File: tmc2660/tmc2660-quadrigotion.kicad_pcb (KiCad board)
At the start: 2 copper layers, 28.4 x 34.7 mm, 16 parts, among them P3 Motor, U1 TMC2660

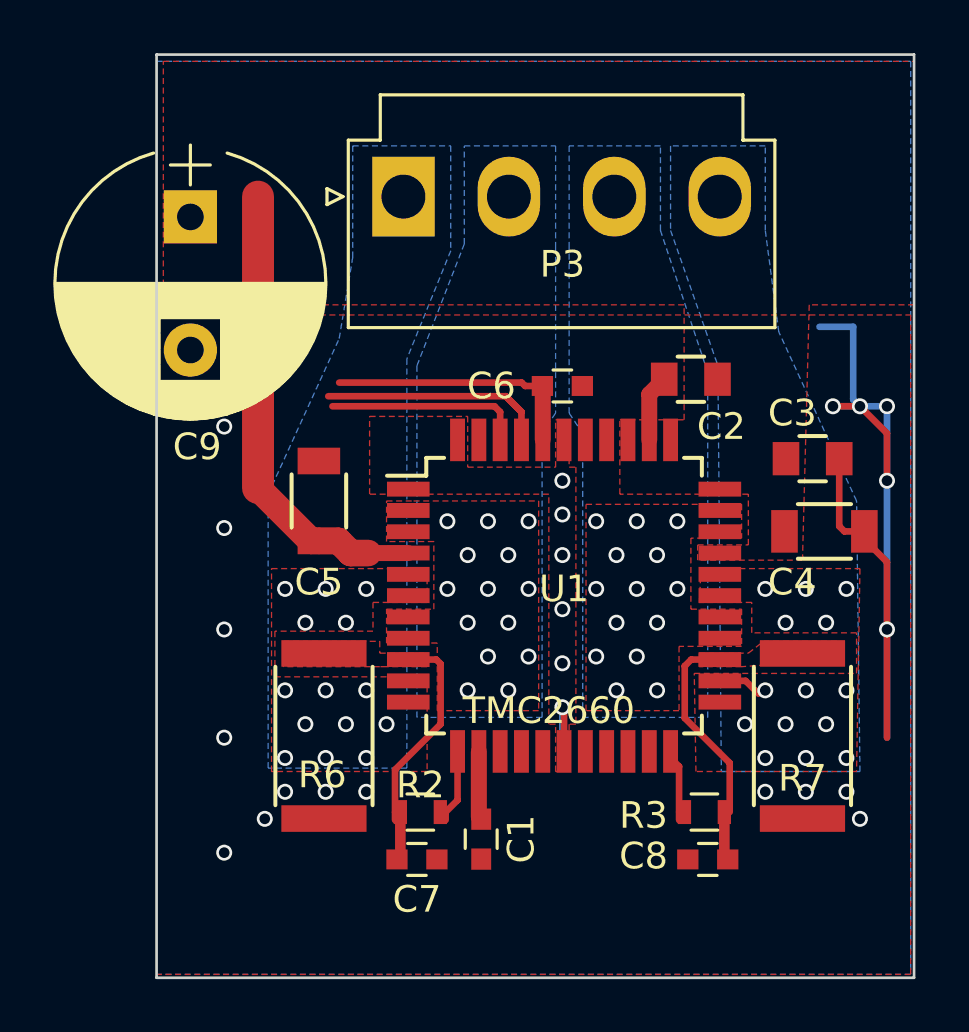
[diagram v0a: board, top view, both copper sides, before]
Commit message: Use smaller connector. JST XH is sufficient for the currents at hand, no need for JST VH
o Also: size adaption. The smaller connector allows to make the board a little
  narrower.
o Add copper pour for VMOT.
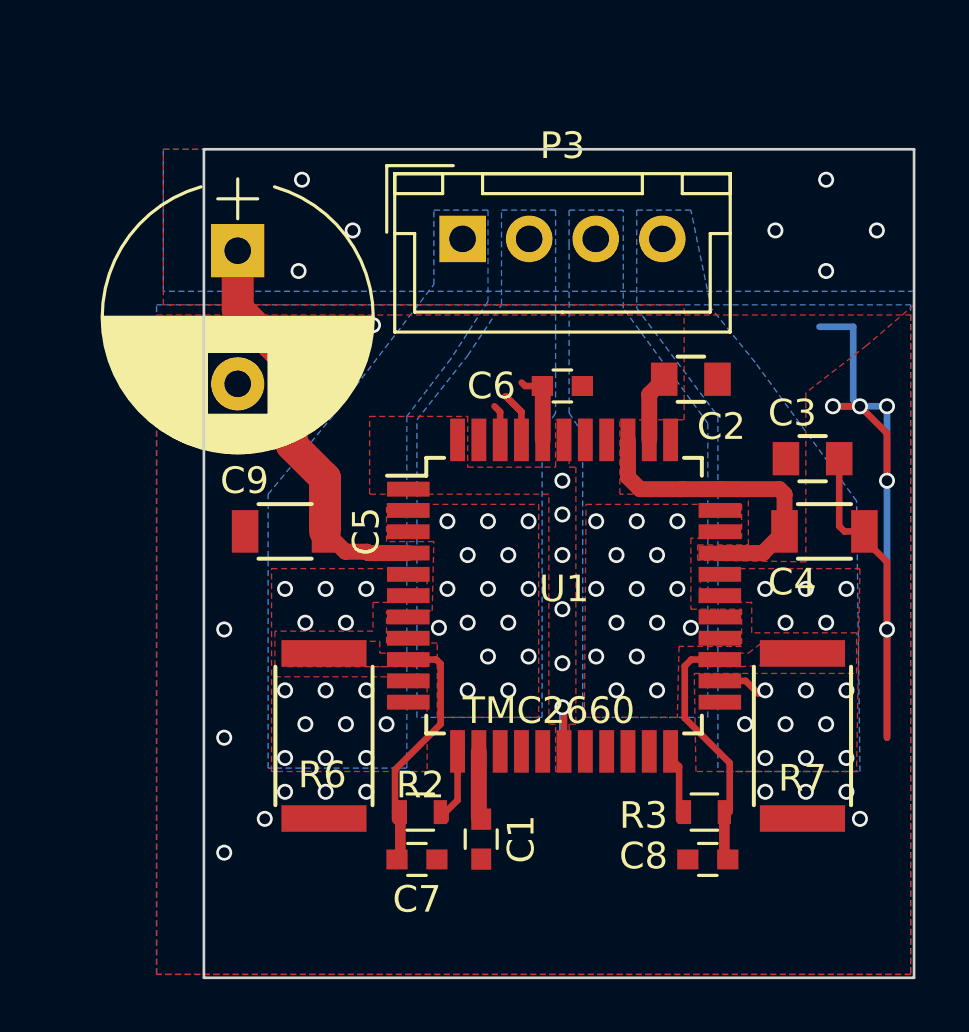
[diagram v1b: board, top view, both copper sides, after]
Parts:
- P3: footprint Connectors_JST:JST_VH_B4P-VH_4x3.96mm_Vertical -> Connectors_JST:JST_XH_B04B-XH-A_04x2.50mm_Straight
- moved P3 2.73 mm to (126.0, 41.0)
- moved C9 2.18 mm to (117.6, 41.4)
- moved C5 1.71 mm to (119.4, 51.9), turned to 180 degrees
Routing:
- net VMot: track 17.6 -> 27.1 mm, vias 0 -> 7
- net VCC: track 9.71 -> 2.86 mm
- net /DIR_1: track 9.39 -> 2.72 mm
- net /STEP_1: track 7.44 -> 1.35 mm
- net GND: vias 25 -> 31
- net 1B1: vias 14 -> 15
- net 1A1: vias 14 -> 15
- added copper zone on B.Cu, net VMot
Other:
- board size 28.4 x 34.7 mm -> 26.7 x 31.1 mm
- net class MotPower added: clearance 0.127, trace_width 0.4, via_dia 0.6, via_drill 0.4

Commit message: Prepare the inner layers.
o Mostly one layer GND and VMOT.
o Have copper fills for all the heatsinking regions to create a good
  heat-conductive connection top to bottom.
o One layer leave mostly free for signals (except VMOT which is
  somewhat out of the way anyway and the heatsinking zones).
o No signals routed yet (probably only going to happen once the
  design is replicated).
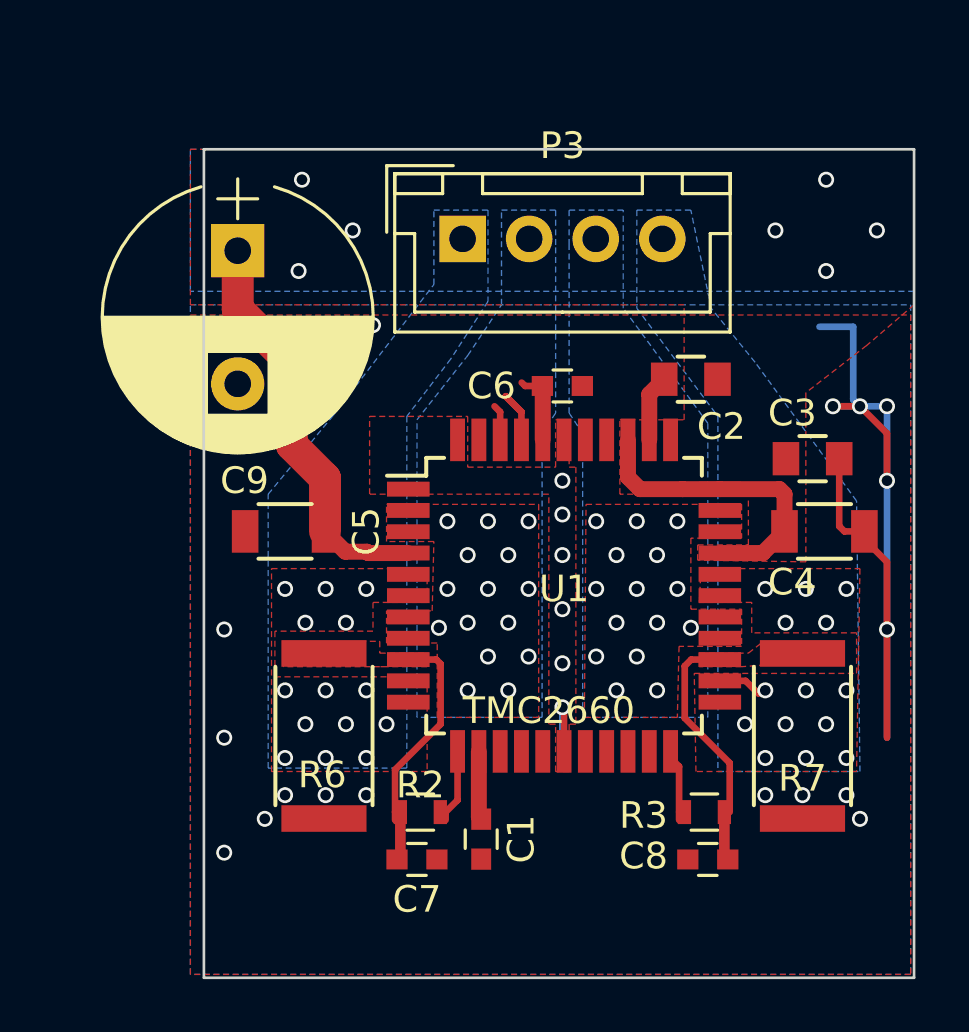
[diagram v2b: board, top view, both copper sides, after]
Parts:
- moved REF** 41.3 mm to (147.3, 65.3)
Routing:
- added copper zone on In1.Cu, net 1A1
- added copper zone on In2.Cu, net 1A1
- added copper zone on In1.Cu, net 1A2
- added copper zone on In2.Cu, net 1A2
- added copper zone on In1.Cu, net 1B1
- added copper zone on In2.Cu, net 1B1
- added copper zone on In1.Cu, net 1B2
- added copper zone on In2.Cu, net 1B2
- added copper zone on In2.Cu, net GND
- added copper zone on In1.Cu, net VMot
- added copper zone on In2.Cu, net VMot
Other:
- copper layers 2 -> 4
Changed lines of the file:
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@@
 (layers
   (0 F.Cu signal)
+  (1 In1.Cu signal)
+  (2 In2.Cu signal)
   (31 B.Cu signal)
   (32 B.Adhes user)
@@
   (user_trace_width 1.2)
   (trace_clearance 0.127)
-  (zone_clearance 0.5)
+  (zone_clearance 0.4)
   (zone_45_only no)
   (trace_min 0.2)
@@
   )
   (module Symbols:Symbol_OSHW-Logo_SilkScreen locked (layer B.Cu)
-    (at 127.762 28.956 270)
+    (at 147.32 65.278 270)
     (descr "Symbol, OSHW-Logo, Silk Screen,")
     (tags "Symbol, OSHW-Logo, Silk Screen,")
@@
     )
   )
-  (gr_text "github.com\nhzeller/quadrigotion" (at 153.416 29.718) (layer B.SilkS)
+  (gr_text "github.com\nhzeller/quadrigotion" (at 146.558 38.608 90) (layer B.SilkS)
     (effects (font (size 1.2 1.2) (thickness 0.25)) (justify left mirror))
   )
@@
   (via (at 117.094 55.626) (size 0.6) (drill 0.4) (layers F.Cu B.Cu) (net 1))
   (via (at 140.97 62.738) (size 0.6) (drill 0.4) (layers F.Cu B.Cu) (net 1))
-  (via (at 140.462 61.722) (size 0.6) (drill 0.4) (layers F.Cu B.Cu) (net 1))
-  (via (at 138.938 61.722) (size 0.6) (drill 0.4) (layers F.Cu B.Cu) (net 1))
-  (via (at 137.414 61.722) (size 0.6) (drill 0.4) (layers F.Cu B.Cu) (net 1))
+  (via (at 140.462 61.849) (size 0.6) (drill 0.4) (layers F.Cu B.Cu) (net 1))
+  (via (at 138.811 61.849) (size 0.6) (drill 0.4) (layers F.Cu B.Cu) (net 1))
+  (via (at 137.414 61.849) (size 0.6) (drill 0.4) (layers F.Cu B.Cu) (net 1))
   (via (at 118.618 62.738) (size 0.6) (drill 0.4) (layers F.Cu B.Cu) (net 1))
-  (via (at 119.38 61.722) (size 0.6) (drill 0.4) (layers F.Cu B.Cu) (net 1))
-  (via (at 120.904 61.722) (size 0.6) (drill 0.4) (layers F.Cu B.Cu) (net 1))
-  (via (at 122.428 61.722) (size 0.6) (drill 0.4) (layers F.Cu B.Cu) (net 1))
+  (via (at 119.38 61.849) (size 0.6) (drill 0.4) (layers F.Cu B.Cu) (net 1))
+  (via (at 120.904 61.849) (size 0.6) (drill 0.4) (layers F.Cu B.Cu) (net 1))
+  (via (at 122.428 61.849) (size 0.6) (drill 0.4) (layers F.Cu B.Cu) (net 1))
   (via (at 129.794 50.038) (size 0.6) (drill 0.4) (layers F.Cu B.Cu) (net 1))
   (via (at 129.794 51.308) (size 0.6) (drill 0.4) (layers F.Cu B.Cu) (net 1))
@@
     (polygon
       (pts
-        (xy 131.953 47.752) (xy 134.366 47.752) (xy 134.366 43.434) (xy 114.808 43.434) (xy 114.808 37.592)
+        (xy 131.953 47.752) (xy 134.366 47.752) (xy 134.366 43.434) (xy 115.824 43.434) (xy 115.824 37.592)
         (xy 143.002 37.592) (xy 143.002 43.434) (xy 141.224 44.958) (xy 138.938 46.736) (xy 138.938 53.086)
         (xy 134.874 53.0225) (xy 134.874 52.451) (xy 136.779 52.451) (xy 136.779 50.546) (xy 131.953 50.546)
@@
     (polygon
       (pts
-        (xy 114.554 43.815) (xy 142.875 43.815) (xy 142.875 68.58) (xy 114.554 68.58)
+        (xy 115.824 43.815) (xy 142.875 43.815) (xy 142.875 68.58) (xy 115.824 68.58)
       )
     )
@@
     (polygon
       (pts
-        (xy 114.554 43.434) (xy 142.875 43.434) (xy 142.875 68.58) (xy 114.554 68.58)
+        (xy 115.824 43.434) (xy 142.875 43.434) (xy 142.875 68.58) (xy 115.824 68.58)
       )
     )
@@
     (polygon
       (pts
-        (xy 114.808 37.592) (xy 143.002 37.592) (xy 143.002 42.926) (xy 114.808 42.926)
-      )
-    )
+        (xy 115.824 37.592) (xy 143.002 37.592) (xy 143.002 42.926) (xy 115.824 42.926)
+      )
+    )
+  )
+  (zone (net 5) (net_name 1A1) (layer In1.Cu) (hatch edge 0.508)
+    (priority 1)
+    (connect_pads yes (clearance 0.4))
+    (min_thickness 0.254)
+    (fill yes (arc_segments 16) (thermal_gap 0.508) (thermal_bridge_width 0.508))
+    (polygon
+      (pts
+        (xy 124.206 50.8) (xy 129.032 50.8) (xy 129.032 60.96) (xy 124.206 60.96)
+      )
+    )
+  )
+  (zone (net 6) (net_name 1A2) (layer In1.Cu) (hatch edge 0.508)
+    (priority 1)
+    (connect_pads yes (clearance 0.4))
+    (min_thickness 0.254)
+    (fill yes (arc_segments 16) (thermal_gap 0.508) (thermal_bridge_width 0.508))
+    (polygon
+      (pts
+        (xy 118.11 53.34) (xy 123.698 53.34) (xy 123.698 60.96) (xy 118.11 60.96)
+      )
+    )
+  )
+  (zone (net 7) (net_name 1B1) (layer In1.Cu) (hatch edge 0.508)
+    (priority 1)
+    (connect_pads yes (clearance 0.4))
+    (min_thickness 0.254)
+    (fill yes (arc_segments 16) (thermal_gap 0.508) (thermal_bridge_width 0.508))
+    (polygon
+      (pts
+        (xy 130.556 50.8) (xy 135.636 50.8) (xy 135.636 60.96) (xy 130.556 60.96)
+      )
+    )
+  )
+  (zone (net 8) (net_name 1B2) (layer In1.Cu) (hatch edge 0.508)
+    (priority 1)
+    (connect_pads yes (clearance 0.4))
+    (min_thickness 0.254)
+    (fill yes (arc_segments 16) (thermal_gap 0.508) (thermal_bridge_width 0.508))
+    (polygon
+      (pts
+        (xy 136.144 53.34) (xy 141.224 53.34) (xy 141.224 60.96) (xy 136.144 60.96)
+      )
+    )
+  )
+  (zone (net 3) (net_name VMot) (layer In2.Cu) (hatch edge 0.508)
+    (connect_pads yes (clearance 0.5))
+    (min_thickness 0.254)
+    (fill yes (arc_segments 16) (thermal_gap 0.508) (thermal_bridge_width 0.508))
+    (polygon
+      (pts
+        (xy 115.824 37.592) (xy 143.002 37.592) (xy 143.002 43.18) (xy 115.824 43.18)
+      )
+    )
+  )
+  (zone (net 1) (net_name GND) (layer In2.Cu) (hatch edge 0.508)
+    (connect_pads yes (clearance 0.3))
+    (min_thickness 0.254)
+    (fill yes (arc_segments 16) (thermal_gap 0.508) (thermal_bridge_width 0.508))
+    (polygon
+      (pts
+        (xy 115.824 43.688) (xy 143.002 43.688) (xy 143.002 68.58) (xy 115.824 68.58)
+      )
+    )
+  )
+  (zone (net 3) (net_name VMot) (layer In1.Cu) (hatch edge 0.508)
+    (connect_pads yes (clearance 0.5))
+    (min_thickness 0.254)
+    (fill yes (arc_segments 16) (thermal_gap 0.508) (thermal_bridge_width 0.508))
+    (polygon
+      (pts
+        (xy 115.824 37.592) (xy 143.002 37.592) (xy 143.002 43.18) (xy 115.824 43.18)
+      )
+    )
+  )
+  (zone (net 7) (net_name 1B1) (layer In2.Cu) (hatch edge 0.508)
+    (priority 1)
+    (connect_pads yes (clearance 0.4))
+    (min_thickness 0.254)
+    (fill yes (arc_segments 16) (thermal_gap 0.508) (thermal_bridge_width 0.508))
+    (polygon
+      (pts
+        (xy 130.556 50.8) (xy 135.636 50.8) (xy 135.636 60.96) (xy 130.556 60.96)
+      )
+    )
+  )
+  (zone (net 8) (net_name 1B2) (layer In2.Cu) (hatch edge 0.508)
+    (priority 1)
+    (connect_pads yes (clearance 0.4))
+    (min_thickness 0.254)
+    (fill yes (arc_segments 16) (thermal_gap 0.508) (thermal_bridge_width 0.508))
+    (polygon
+      (pts
+        (xy 136.144 53.34) (xy 141.224 53.34) (xy 141.224 60.96) (xy 136.144 60.96)
+      )
+    )
+  )
+  (zone (net 6) (net_name 1A2) (layer In2.Cu) (hatch edge 0.508)
+    (priority 1)
+    (connect_pads yes (clearance 0.4))
+    (min_thickness 0.254)
+    (fill yes (arc_segments 16) (thermal_gap 0.508) (thermal_bridge_width 0.508))
+    (polygon
+      (pts
+        (xy 118.11 53.34) (xy 123.698 53.34) (xy 123.698 60.96) (xy 118.11 60.96)
+      )
+    )
+  )
+  (zone (net 5) (net_name 1A1) (layer In2.Cu) (hatch edge 0.508)
+    (priority 1)
+    (connect_pads yes (clearance 0.4))
+    (min_thickness 0.254)
+    (fill yes (arc_segments 16) (thermal_gap 0.508) (thermal_bridge_width 0.508))
+    (polygon
+      (pts
+        (xy 124.206 50.8) (xy 129.032 50.8) (xy 129.032 60.96) (xy 124.206 60.96)
+      )
+    )
